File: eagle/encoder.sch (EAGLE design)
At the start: 11 parts, among them IC1 LM339D, U1 MCP42XXX

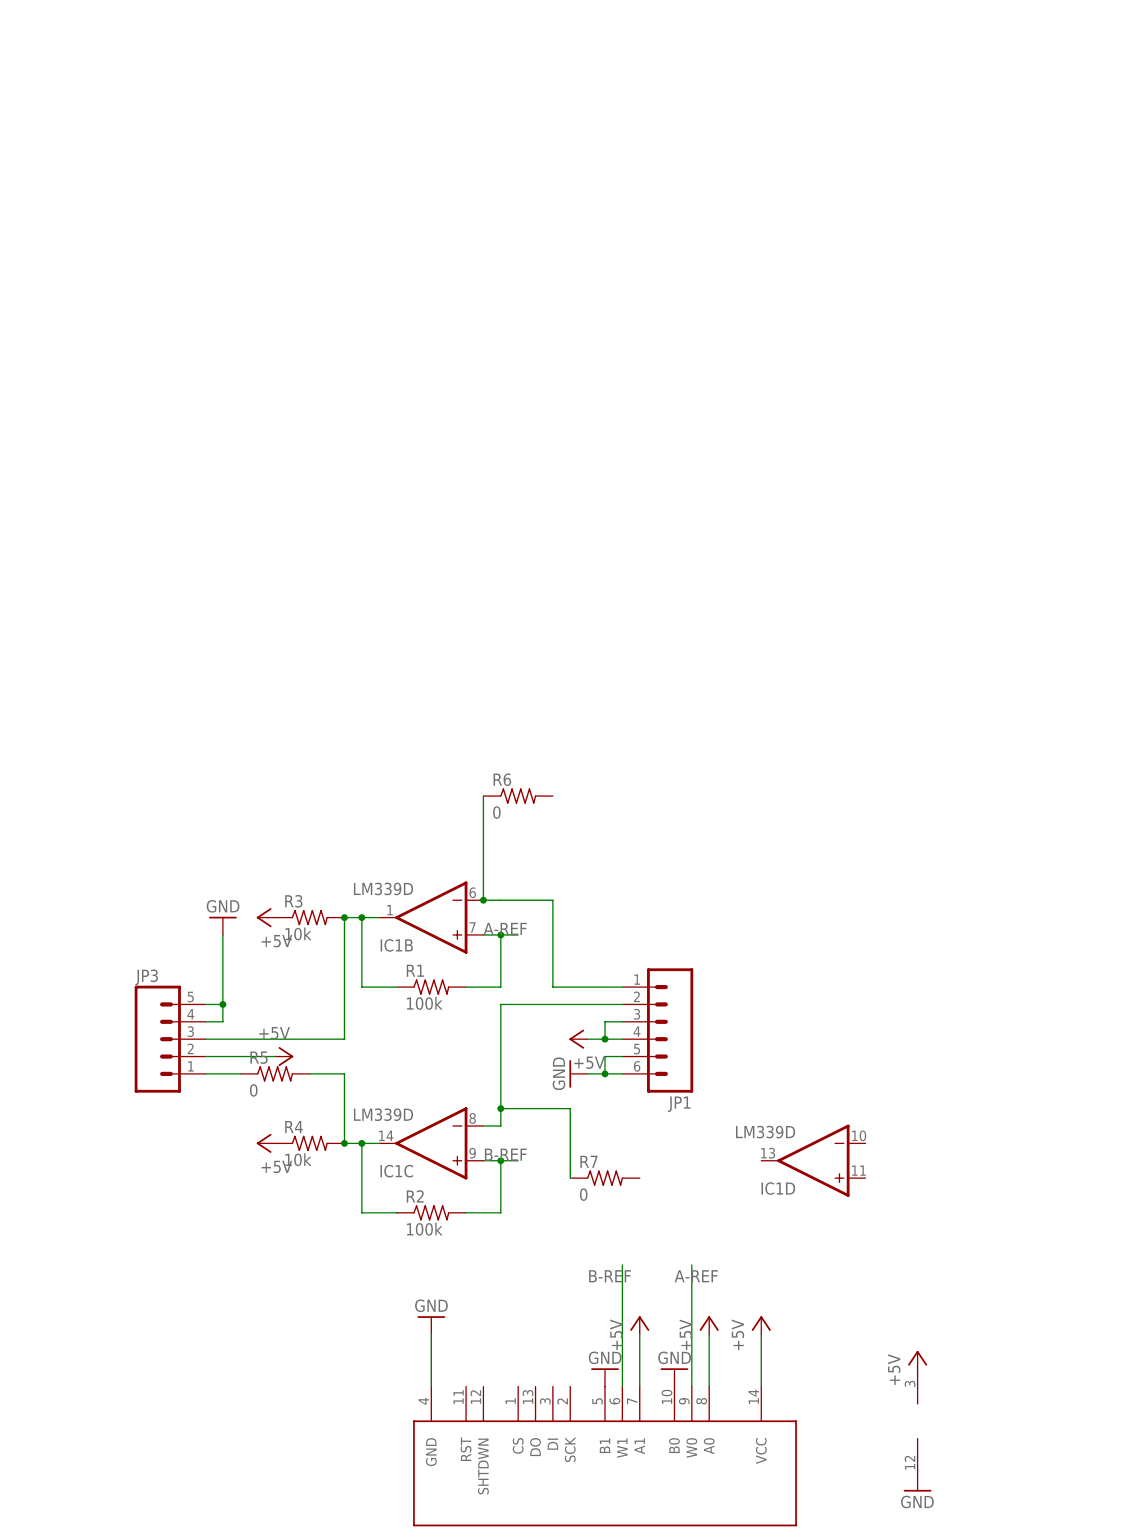
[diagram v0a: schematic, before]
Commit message: Added atmega.
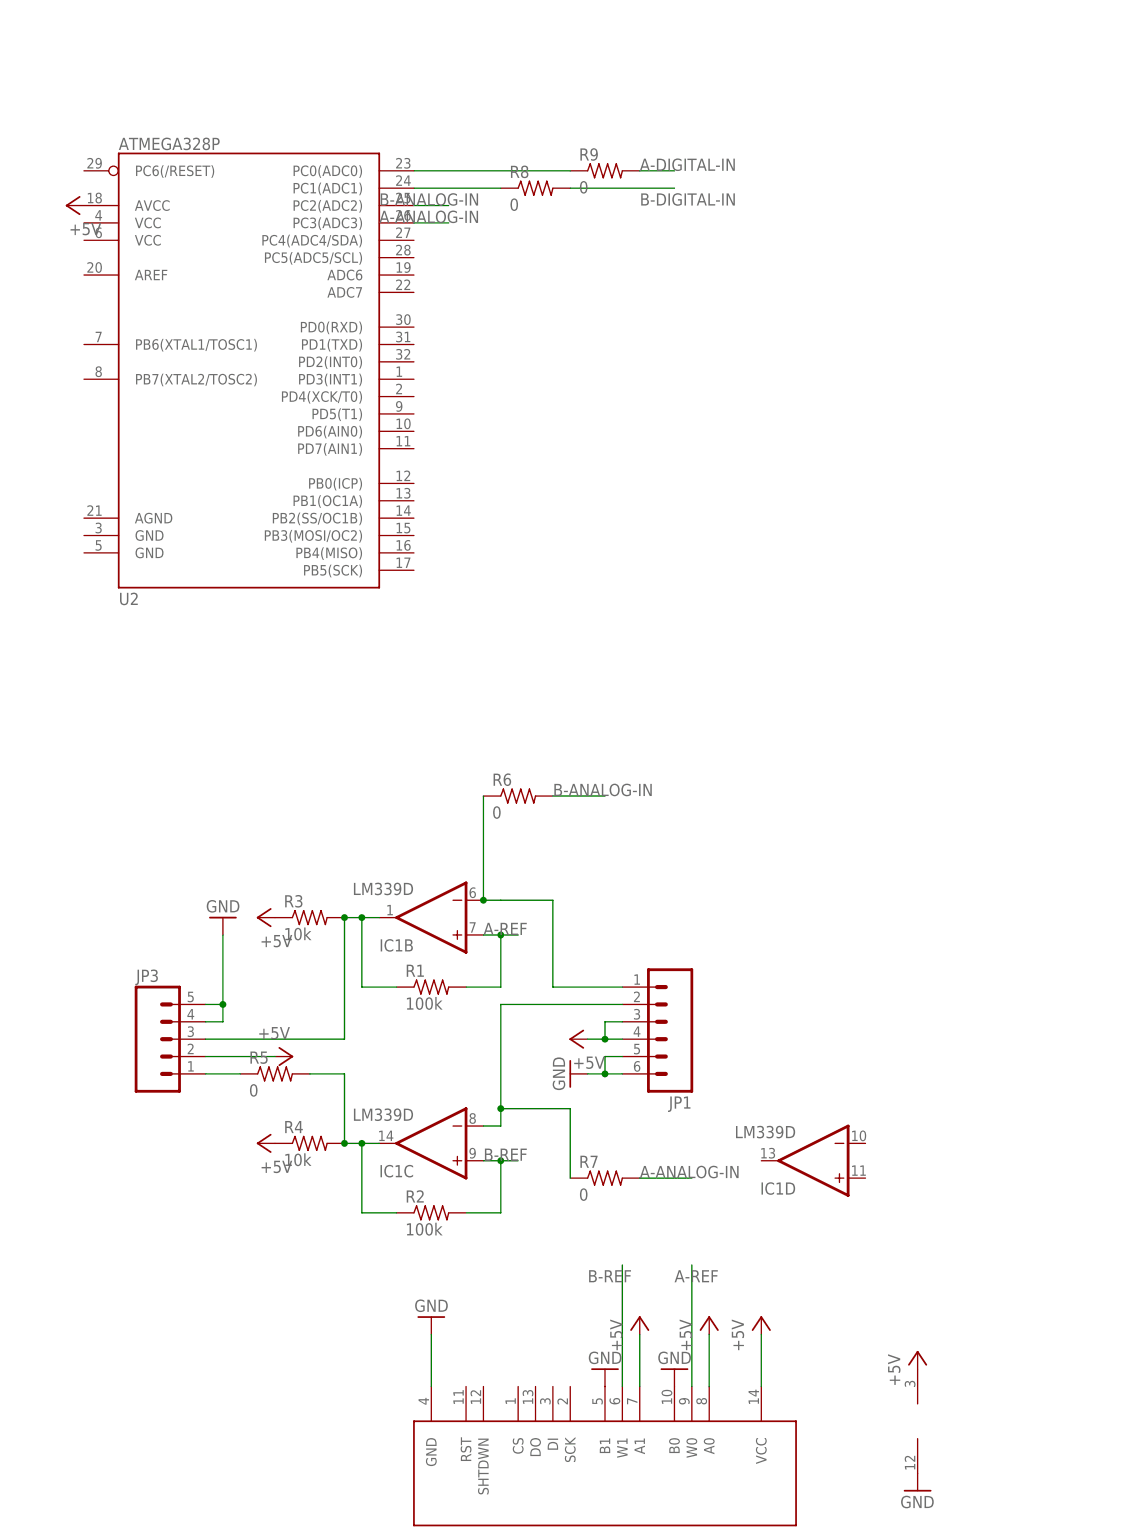
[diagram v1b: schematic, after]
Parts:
- added R8, R9: 0, resistor:R-US_R1206
- added U2: ATMEGA328P, SparkFun-DigitalIC:ATMEGA328_SMT
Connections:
- removed net N$2: IC1B.OUT, JP3.3, R1.1, R3.2
- removed net N$4: JP3.1, R5.1
- new net A-ANALOG-IN: R7.2, U2.PC3(ADC3)
- new net A-DIGITAL-IN: IC1B.OUT, JP3.3, R1.1, R3.2, R9.2
- new net B-ANALOG-IN: R6.2, U2.PC2(ADC2)
- new net B-DIGITAL-IN: JP3.1, R5.1, R8.2
- new net N$6: R8.1, U2.PC1(ADC1)
- new net N$7: R9.1, U2.PC0(ADC0)
- net +5V: now also U2.AVCC

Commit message: Added SPI hookup
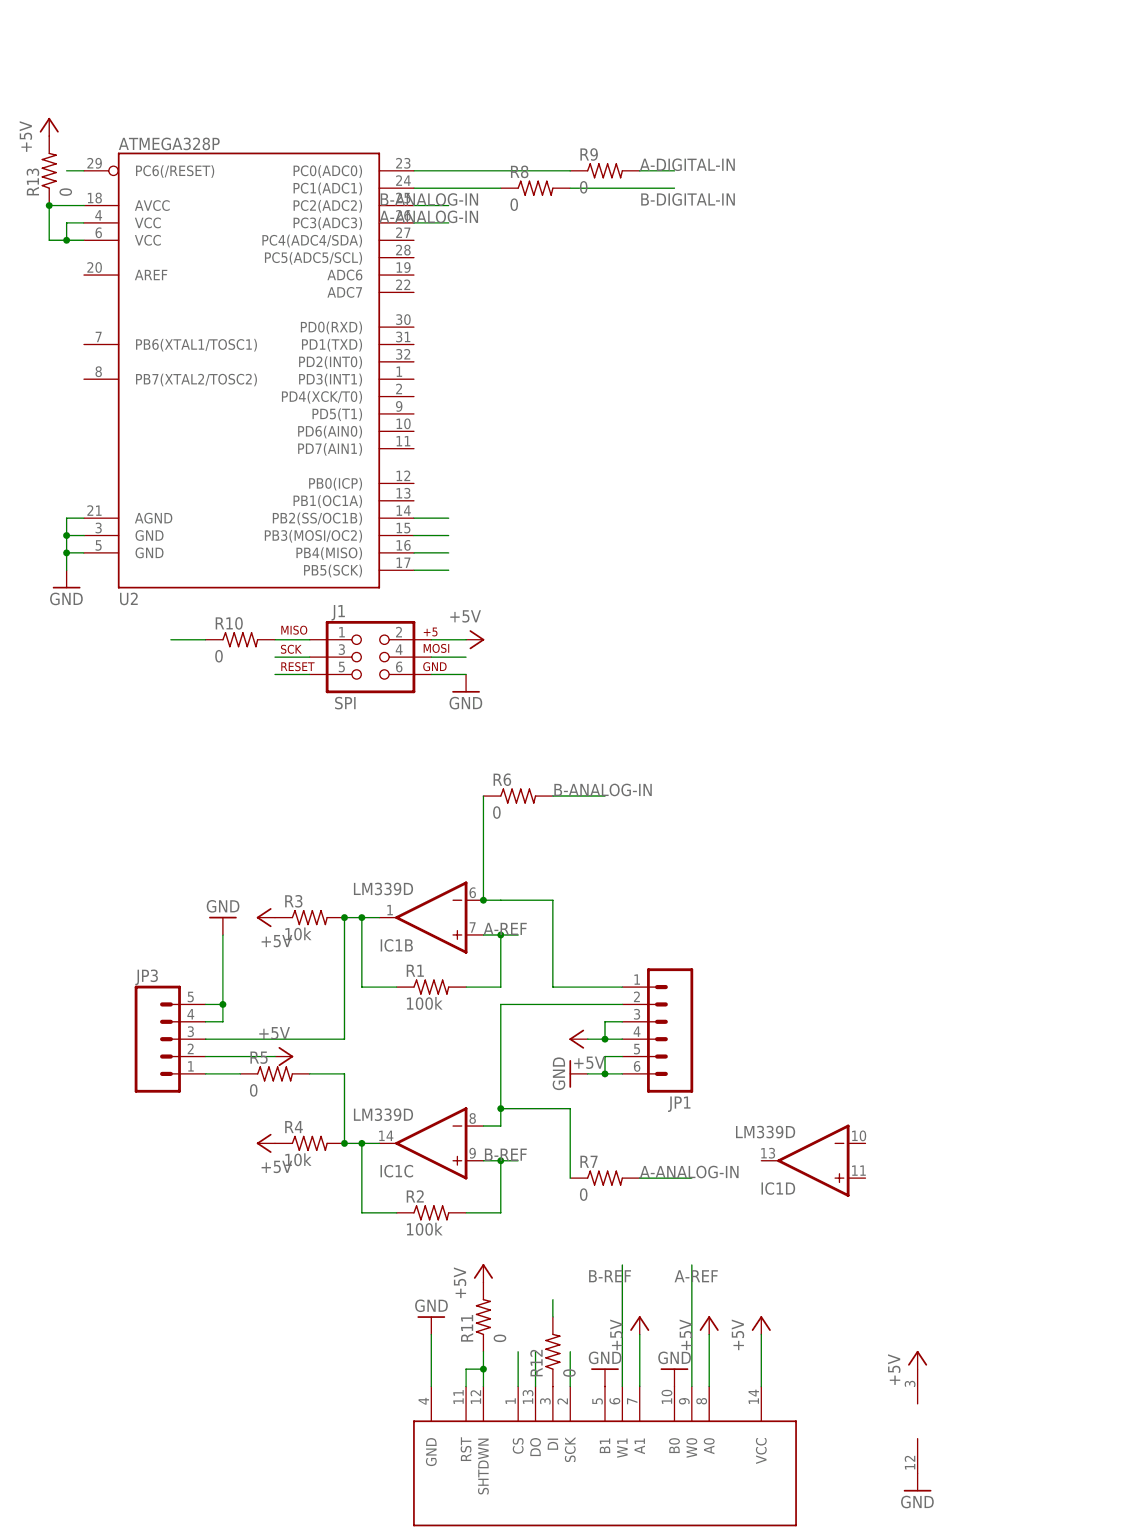
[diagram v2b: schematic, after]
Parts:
- added J1: SPI, SparkFun-Connectors:AVR_SPI_PRG_6NS
- added R10, R11, R12, R13: 0, resistor:R-US_R1206
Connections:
- new net MISO: R10.1, U1.DO, U2.PB4(MISO)
- new net MOSI: J1.4, R12.2, U2.PB3(MOSI/OC2)
- new net N$2: J1.1, R10.2
- new net N$4: R11.1, U1.RST, U1.SHTDWN
- new net N$8: R12.1, U1.DI
- new net N$9: R13.1, U2.AVCC, U2.VCC@1, U2.VCC@2
- new net RESET: J1.5, U2.PC6(/RESET)
- new net SCK: J1.3, U1.SCK, U2.PB5(SCK)
- new net SS: U1.CS, U2.PB2(SS/OC1B)
- net +5V: now also J1.2, R11.2, R13.2; no longer U2.AVCC
- net GND: now also J1.6, U2.AGND, U2.GND@1, U2.GND@2
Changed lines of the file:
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@@
 <part name="R8" library="resistor" deviceset="R-US_" device="R1206" value="0"/>
 <part name="R9" library="resistor" deviceset="R-US_" device="R1206" value="0"/>
-<part name="P+9" library="supply1" deviceset="+5V" device=""/>
+<part name="R10" library="resistor" deviceset="R-US_" device="R1206" value="0"/>
+<part name="J1" library="SparkFun-Connectors" deviceset="AVR_SPI_PRG_6" device="NS" value="SPI"/>
+<part name="P+11" library="supply1" deviceset="+5V" device=""/>
+<part name="GND8" library="supply1" deviceset="GND" device=""/>
+<part name="GND6" library="supply1" deviceset="GND" device=""/>
+<part name="R11" library="resistor" deviceset="R-US_" device="R1206" value="0"/>
+<part name="P+10" library="supply1" deviceset="+5V" device=""/>
+<part name="R12" library="resistor" deviceset="R-US_" device="R1206" value="0"/>
+<part name="R13" library="resistor" deviceset="R-US_" device="R1206" value="0"/>
+<part name="P+12" library="supply1" deviceset="+5V" device=""/>
 </parts>
 <sheets>
@@
 <instance part="R8" gate="G$1" x="68.58" y="200.66"/>
 <instance part="R9" gate="G$1" x="78.74" y="203.2"/>
-<instance part="P+9" gate="1" x="0" y="198.12" rot="R90"/>
+<instance part="R10" gate="G$1" x="25.4" y="134.62"/>
+<instance part="J1" gate="G$1" x="43.18" y="132.08"/>
+<instance part="P+11" gate="1" x="60.96" y="134.62" rot="R270"/>
+<instance part="GND8" gate="1" x="58.42" y="127"/>
+<instance part="GND6" gate="1" x="0" y="142.24"/>
+<instance part="R11" gate="G$1" x="60.96" y="35.56" rot="R90"/>
+<instance part="P+10" gate="1" x="60.96" y="43.18"/>
+<instance part="R12" gate="G$1" x="71.12" y="30.48" rot="R90"/>
+<instance part="R13" gate="G$1" x="-2.54" y="203.2" rot="R90"/>
+<instance part="P+12" gate="1" x="-2.54" y="210.82"/>
 </instances>
 <busses>
@@
 </segment>
 <segment>
-<pinref part="U2" gate="G$1" pin="AVCC"/>
-<pinref part="P+9" gate="1" pin="+5V"/>
+<pinref part="J1" gate="G$1" pin="2"/>
+<wire x1="53.34" y1="134.62" x2="58.42" y2="134.62" width="0.1524" layer="91"/>
+<pinref part="P+11" gate="1" pin="+5V"/>
+</segment>
+<segment>
+<pinref part="R11" gate="G$1" pin="2"/>
+<pinref part="P+10" gate="1" pin="+5V"/>
+</segment>
+<segment>
+<pinref part="R13" gate="G$1" pin="2"/>
+<pinref part="P+12" gate="1" pin="+5V"/>
 </segment>
 </net>
@@
 <wire x1="22.86" y1="81.28" x2="22.86" y2="91.44" width="0.1524" layer="91"/>
 <junction x="22.86" y="81.28"/>
+</segment>
+<segment>
+<pinref part="J1" gate="G$1" pin="6"/>
+<wire x1="53.34" y1="129.54" x2="58.42" y2="129.54" width="0.1524" layer="91"/>
+<pinref part="GND8" gate="1" pin="GND"/>
+</segment>
+<segment>
+<pinref part="U2" gate="G$1" pin="AGND"/>
+<wire x1="2.54" y1="152.4" x2="0" y2="152.4" width="0.1524" layer="91"/>
+<wire x1="0" y1="152.4" x2="0" y2="149.86" width="0.1524" layer="91"/>
+<pinref part="U2" gate="G$1" pin="GND@1"/>
+<wire x1="0" y1="149.86" x2="0" y2="147.32" width="0.1524" layer="91"/>
+<wire x1="0" y1="147.32" x2="0" y2="144.78" width="0.1524" layer="91"/>
+<wire x1="2.54" y1="149.86" x2="0" y2="149.86" width="0.1524" layer="91"/>
+<pinref part="U2" gate="G$1" pin="GND@2"/>
+<wire x1="2.54" y1="147.32" x2="0" y2="147.32" width="0.1524" layer="91"/>
+<pinref part="GND6" gate="1" pin="GND"/>
+<junction x="0" y="149.86"/>
+<junction x="0" y="147.32"/>
 </segment>
 </net>
@@
 </segment>
 </net>
+<net name="MOSI" class="0">
+<segment>
+<pinref part="U2" gate="G$1" pin="PB3(MOSI/OC2)"/>
+<wire x1="50.8" y1="149.86" x2="55.88" y2="149.86" width="0.1524" layer="91"/>
+</segment>
+<segment>
+<pinref part="J1" gate="G$1" pin="4"/>
+<wire x1="53.34" y1="132.08" x2="58.42" y2="132.08" width="0.1524" layer="91"/>
+</segment>
+<segment>
+<pinref part="R12" gate="G$1" pin="2"/>
+<wire x1="71.12" y1="35.56" x2="71.12" y2="38.1" width="0.1524" layer="91"/>
+</segment>
+</net>
+<net name="MISO" class="0">
+<segment>
+<pinref part="U1" gate="G$1" pin="DO"/>
+<wire x1="68.58" y1="25.4" x2="68.58" y2="30.48" width="0.1524" layer="91"/>
+</segment>
+<segment>
+<pinref part="U2" gate="G$1" pin="PB4(MISO)"/>
+<wire x1="50.8" y1="147.32" x2="55.88" y2="147.32" width="0.1524" layer="91"/>
+</segment>
+<segment>
+<pinref part="R10" gate="G$1" pin="1"/>
+<wire x1="20.32" y1="134.62" x2="15.24" y2="134.62" width="0.1524" layer="91"/>
+</segment>
+</net>
+<net name="SCK" class="0">
+<segment>
+<pinref part="U2" gate="G$1" pin="PB5(SCK)"/>
+<wire x1="50.8" y1="144.78" x2="55.88" y2="144.78" width="0.1524" layer="91"/>
+</segment>
+<segment>
+<pinref part="U1" gate="G$1" pin="SCK"/>
+<wire x1="73.66" y1="25.4" x2="73.66" y2="30.48" width="0.1524" layer="91"/>
+</segment>
+<segment>
+<pinref part="J1" gate="G$1" pin="3"/>
+<wire x1="35.56" y1="132.08" x2="30.48" y2="132.08" width="0.1524" layer="91"/>
+</segment>
+</net>
+<net name="RESET" class="0">
+<segment>
+<pinref part="U2" gate="G$1" pin="PC6(/RESET)"/>
+<wire x1="2.54" y1="203.2" x2="0" y2="203.2" width="0.1524" layer="91"/>
+</segment>
+<segment>
+<pinref part="J1" gate="G$1" pin="5"/>
+<wire x1="35.56" y1="129.54" x2="30.48" y2="129.54" width="0.1524" layer="91"/>
+</segment>
+</net>
+<net name="SS" class="0">
+<segment>
+<pinref part="U1" gate="G$1" pin="CS"/>
+<wire x1="66.04" y1="25.4" x2="66.04" y2="30.48" width="0.1524" layer="91"/>
+</segment>
+<segment>
+<pinref part="U2" gate="G$1" pin="PB2(SS/OC1B)"/>
+<wire x1="50.8" y1="152.4" x2="55.88" y2="152.4" width="0.1524" layer="91"/>
+</segment>
+</net>
+<net name="N$2" class="0">
+<segment>
+<pinref part="J1" gate="G$1" pin="1"/>
+<pinref part="R10" gate="G$1" pin="2"/>
+<wire x1="30.48" y1="134.62" x2="35.56" y2="134.62" width="0.1524" layer="91"/>
+</segment>
+</net>
+<net name="N$4" class="0">
+<segment>
+<pinref part="U1" gate="G$1" pin="RST"/>
+<wire x1="58.42" y1="25.4" x2="58.42" y2="27.94" width="0.1524" layer="91"/>
+<pinref part="U1" gate="G$1" pin="SHTDWN"/>
+<wire x1="58.42" y1="27.94" x2="60.96" y2="27.94" width="0.1524" layer="91"/>
+<wire x1="60.96" y1="25.4" x2="60.96" y2="27.94" width="0.1524" layer="91"/>
+<junction x="60.96" y="27.94"/>
+<wire x1="60.96" y1="27.94" x2="60.96" y2="30.48" width="0.1524" layer="91"/>
+<pinref part="R11" gate="G$1" pin="1"/>
+</segment>
+</net>
+<net name="N$8" class="0">
+<segment>
+<pinref part="U1" gate="G$1" pin="DI"/>
+<pinref part="R12" gate="G$1" pin="1"/>
+</segment>
+</net>
+<net name="N$9" class="0">
+<segment>
+<pinref part="U2" gate="G$1" pin="VCC@2"/>
+<wire x1="2.54" y1="193.04" x2="0" y2="193.04" width="0.1524" layer="91"/>
+<wire x1="0" y1="193.04" x2="0" y2="195.58" width="0.1524" layer="91"/>
+<pinref part="U2" gate="G$1" pin="VCC@1"/>
+<wire x1="2.54" y1="195.58" x2="0" y2="195.58" width="0.1524" layer="91"/>
+<wire x1="0" y1="193.04" x2="-2.54" y2="193.04" width="0.1524" layer="91"/>
+<pinref part="U2" gate="G$1" pin="AVCC"/>
+<wire x1="-2.54" y1="198.12" x2="2.54" y2="198.12" width="0.1524" layer="91"/>
+<pinref part="R13" gate="G$1" pin="1"/>
+<wire x1="-2.54" y1="193.04" x2="-2.54" y2="198.12" width="0.1524" layer="91"/>
+<junction x="-2.54" y="198.12"/>
+<junction x="0" y="193.04"/>
+</segment>
+</net>
